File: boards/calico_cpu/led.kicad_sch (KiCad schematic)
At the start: 96 parts

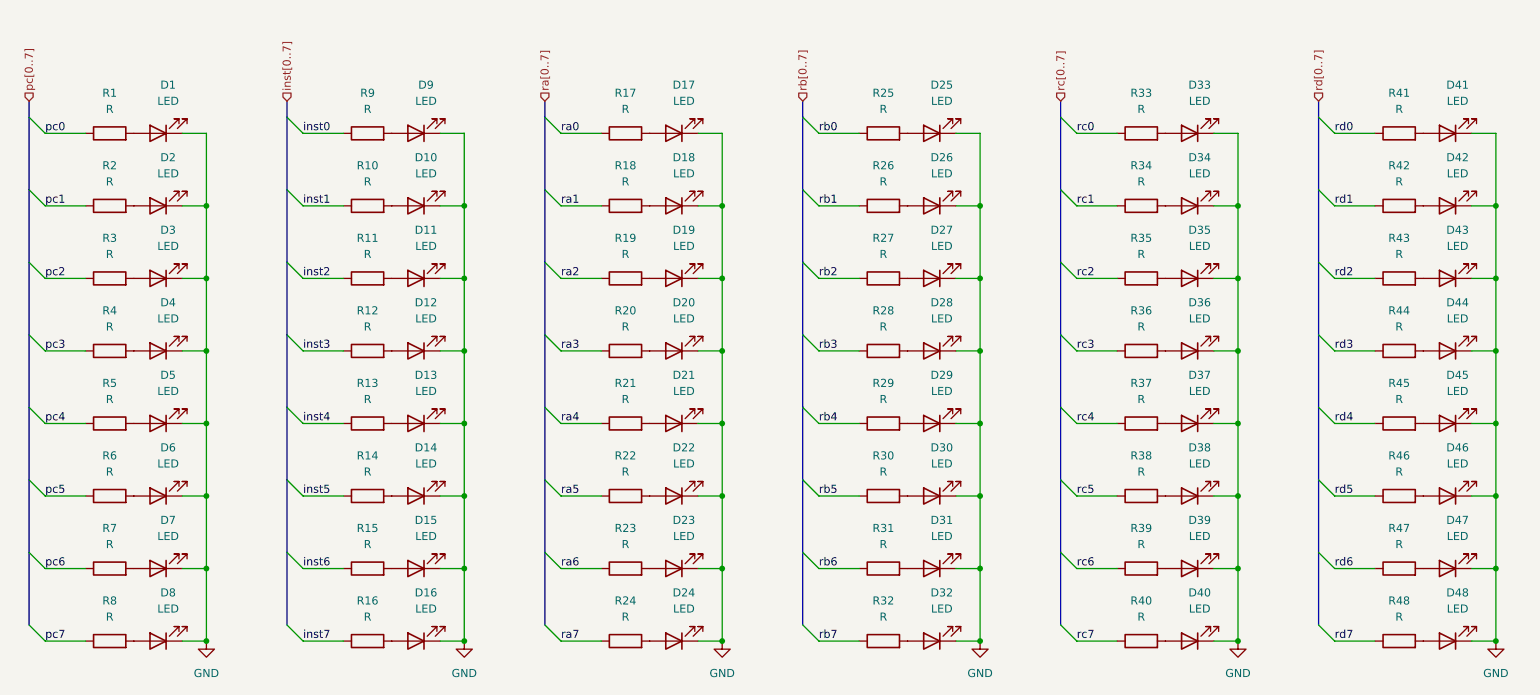
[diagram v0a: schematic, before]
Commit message: set LED and resistors
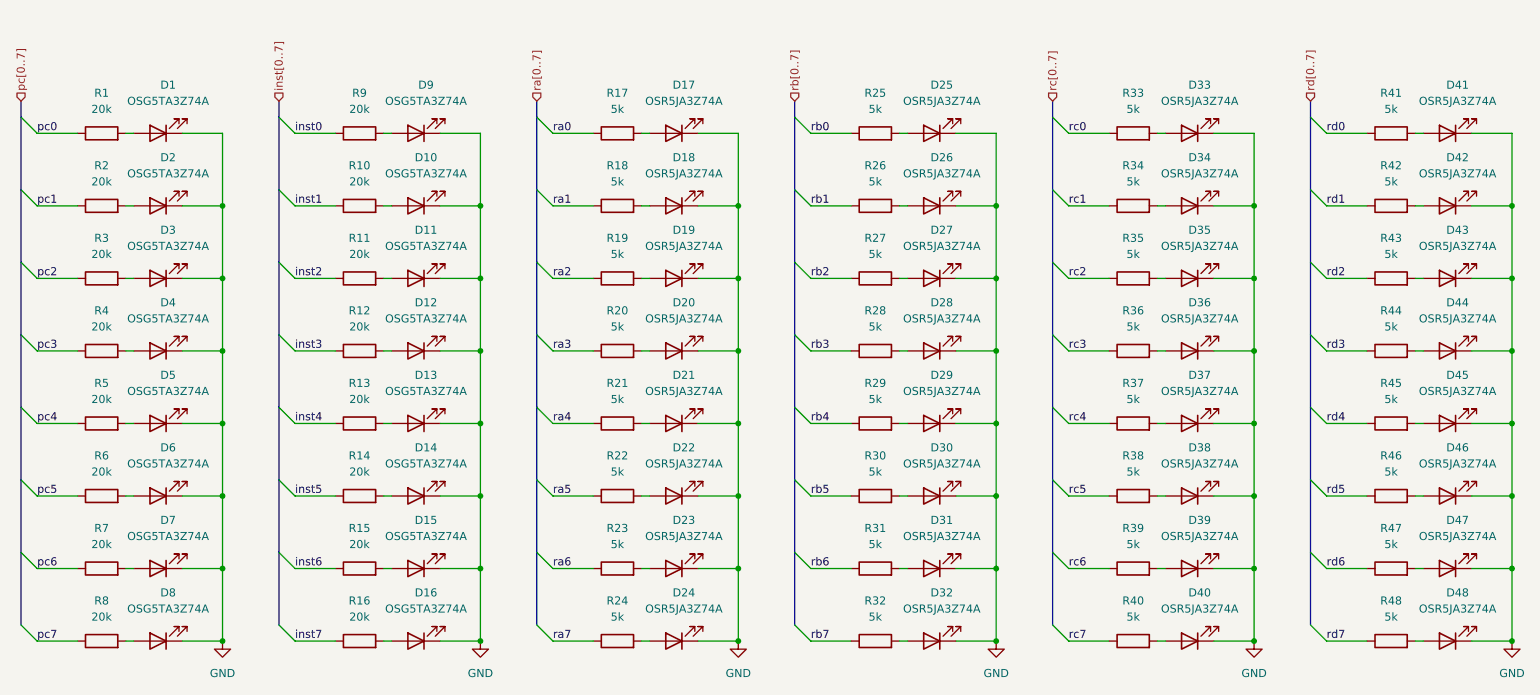
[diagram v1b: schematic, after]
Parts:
- D1, D10, D11, D12, D13, D14, D15, D16, D2, D3, D4, D5, D6, D7, D8, D9: value LED -> OSG5TA3Z74A
- D17, D18, D19, D20, D21, D22, D23, D24, D25, D26, D27, D28, D29, D30, D31, D32, D33, D34, D35, D36, D37, D38, D39, D40, D41, D42, D43, D44, D45, D46, D47, D48: value LED -> OSR5JA3Z74A
- R1, R10, R11, R12, R13, R14, R15, R16, R2, R3, R4, R5, R6, R7, R8, R9: value R -> 20k
- R17, R18, R19, R20, R21, R22, R23, R24, R25, R26, R27, R28, R29, R30, R31, R32, R33, R34, R35, R36, R37, R38, R39, R40, R41, R42, R43, R44, R45, R46, R47, R48: value R -> 5k
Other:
- moved on the sheet: R1, R10, R11, R12, R13, R14, R15, R16, R17, R18, R19, R2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

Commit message: change values according to actual parts
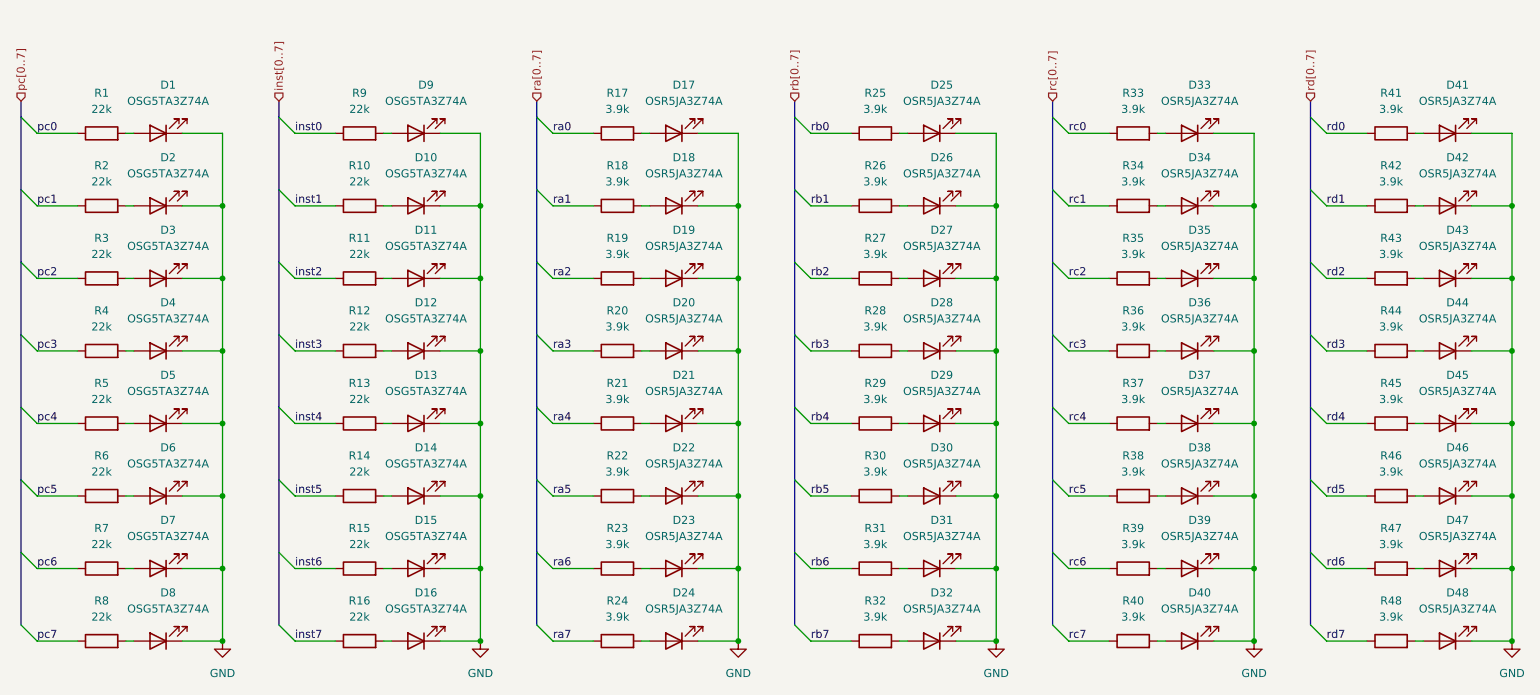
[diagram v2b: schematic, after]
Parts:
- R1, R10, R11, R12, R13, R14, R15, R16, R2, R3, R4, R5, R6, R7, R8, R9: value 20k -> 22k
- R17, R18, R19, R20, R21, R22, R23, R24, R25, R26, R27, R28, R29, R30, R31, R32, R33, R34, R35, R36, R37, R38, R39, R40, R41, R42, R43, R44, R45, R46, R47, R48: value 5k -> 3.9k
